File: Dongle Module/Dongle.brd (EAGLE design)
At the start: 100 x 50 mm, 74 parts, among them Q2 2.5A/30V, U1 RFM69HCW, U10 74AHC1G125, U2 HALL-EFFECTSMD, U3 HALL-EFFECTSMD, U4 HALL-EFFECTSMD, U5 HALL-EFFECTSMD, U6 BQ27441-G1, U7 BQ24075, U8 ATSAMD21G-A, U9 3.3V, Y1 32.768kHz

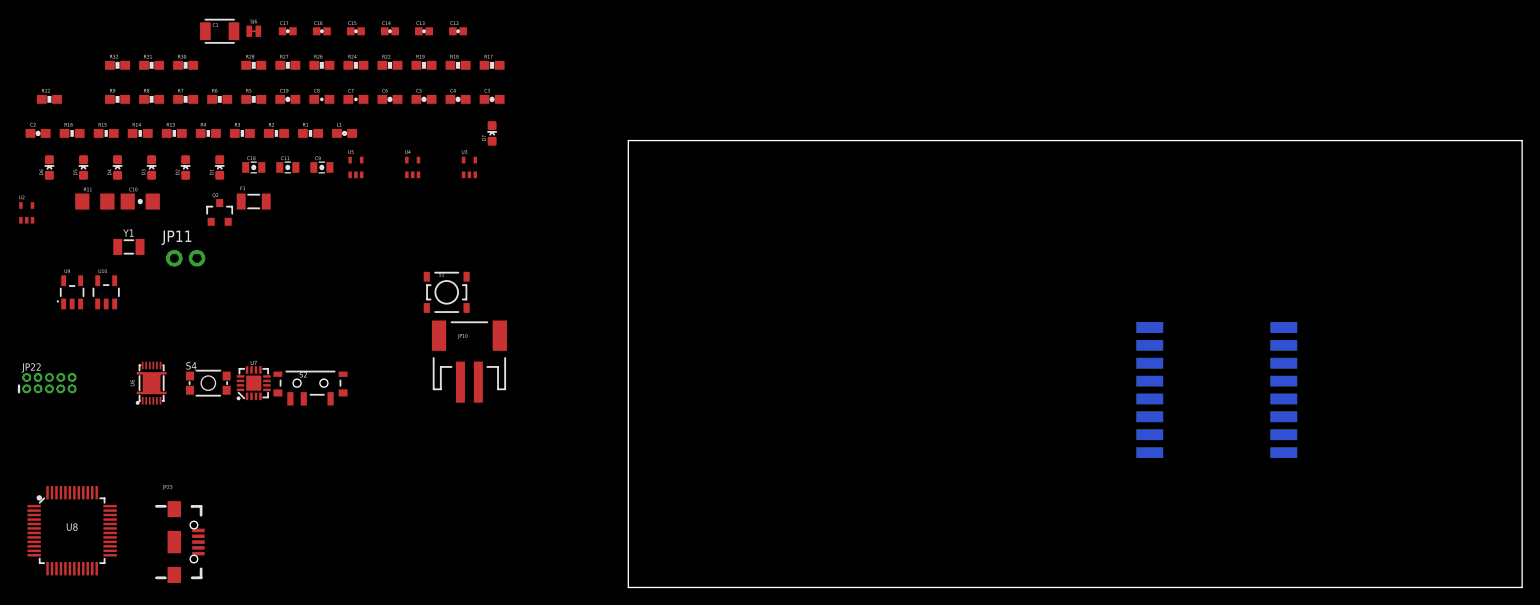
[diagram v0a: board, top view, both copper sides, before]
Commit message: Worked on the laser and dongle schematics Placed the parts on the laser and dongle boards in their rough locations
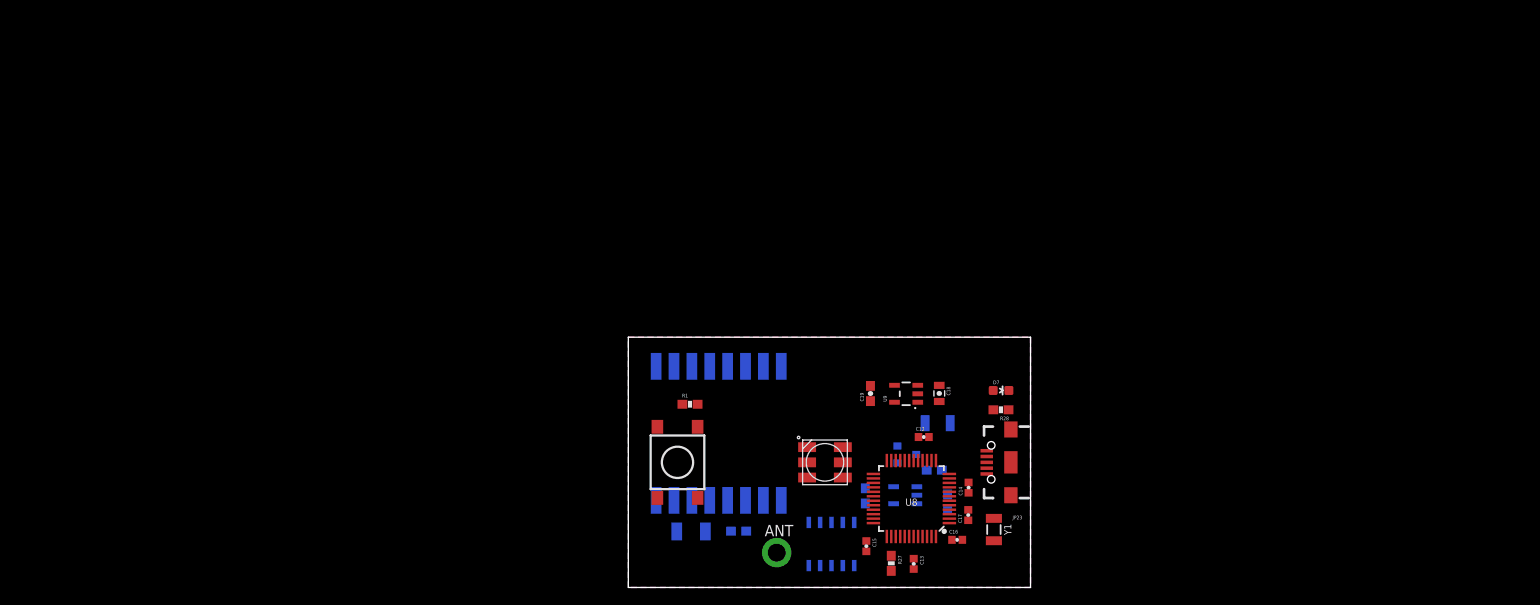
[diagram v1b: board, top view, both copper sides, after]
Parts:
- removed C10: 1.0uF, SparkFun-Capacitors:1206-CAP
- removed C11, C9: 10uF, SparkFun-Capacitors:0805-CAP
- removed C3, C4, C5, C6: 0.1uF, SparkFun-Capacitors:0603-CAP@1
- removed C7: 1.0uF, SparkFun-Capacitors:0603-CAP@2
- removed C8: 0.47uF, SparkFun-Capacitors:0603-CAP@2
- removed D1: BLU, SparkFun-LED:LED-0603
- removed D2, D6: RED, SparkFun-LED:LED-0603
- removed D3: GREEN, SparkFun-LED:LED-0603
- removed D4: WHT, SparkFun-LED:LED-0603
- removed D5: BLUE, SparkFun-LED:LED-0603
- removed JP10: (no value), SparkFun-Connectors:JST-2-SMD
- removed JP11: (no value), mike-temp:1X02_NO_SILK
- removed L1: FB - 30Ohm, SparkFun-Passives:0603
- removed R11: 0.01, SparkFun-Resistors:1206
- removed R12: 1.1k, SparkFun-Passives:0603-RES
- removed R13, R14: 4.7K, SparkFun-Resistors:0603-RES@2
- removed R15, R2, R3, R4: 180, SparkFun-Resistors:0603-RES@2
- removed R16: 1K, SparkFun-Resistors:0603-RES@2
- removed R17, R24: 100k, SparkFun-Resistors:0603-RES
- removed R18, R19, R22, R26: 10K, SparkFun-Resistors:0603-RES
- removed R5, R6, R7, R8, R9: 10K, SparkFun-Resistors:0603-RES@1
- removed S2: (no value), SparkFun-Electromechanical:SWITCH-SPST-SMD-A
- removed S4: RESET, samd21-temp:TACTILE_SWITCH_SMD_4.6X2.8MM
- removed SJ6: PWR-LED, SparkFun-Passives:PAD-JUMPER-2-NC_BY_TRACE_NO_SILK
- removed U2, U3, U4, U5: HALL-EFFECTSMD, SparkFun-Sensors:SC70
- removed U6: BQ27441-G1, battery-management-temp:PDSO-N12
- removed U7: BQ24075, battery-management-temp:PVQFN-N16
- added ANT: (no value), SparkFun-Connectors:1X01_2MM
- added U$1: APA102, SAUVE:APA102
- JP22: value CORTEX_DEBUGPTH -> CORTEX_DEBUGSMD; device samd21-temp:2X5-PTH-1.27MM -> SparkFun-Connectors:SAMTECH_FTSH-105-01
- R1: value 180 -> 330; device SparkFun-Resistors:0603-RES@2 -> SparkFun-Resistors:0603-RES
- S1: value SWITCH-MOMENTARY-2SMD-2 -> SWITCH-MOMENTARY-2SMD-4; device SparkFun-Electromechanical:TACTILE_SWITCH_SMD-2 -> SparkFun-Electromechanical:TACTILE_SWITCH_TALL
- moved Y1 101.8 mm to (40.9, 6.48), turned to 270 degrees
- moved R31 101.6 mm to (35.7, 9.56), flipped to the bottom, turned to 90 degrees
- moved R32 96.5 mm to (26.5, 10.2), flipped to the bottom, turned to 90 degrees
- moved R30 95.2 mm to (34.2, 13.1), flipped to the bottom
- moved JP23 94.0 mm to (42.8, 14.0), turned to 180 degrees
- moved U9 94.0 mm to (31.1, 21.7), turned to 90 degrees
- moved U8 94.0 mm to (31.7, 9.95), turned to 180 degrees
- moved C17 93.4 mm to (38.0, 8.10), turned to 90 degrees
- moved U10 92.2 mm to (31.0, 10.3), flipped to the bottom, turned to 270 degrees
- moved R28 92.1 mm to (41.7, 19.9), turned to 180 degrees
- moved C16 91.0 mm to (36.8, 5.33)
- moved C2 90.1 mm to (12.3, 6.30), flipped to the bottom, turned to 180 degrees
- moved JP22 89.3 mm to (22.7, 4.86), flipped to the bottom
- moved R27 87.5 mm to (29.4, 2.70), turned to 270 degrees
- moved C14 82.5 mm to (38.1, 11.2), turned to 90 degrees
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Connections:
- removed net !CE!: R17.1, U7.4
- removed net !CHG!: R15.2, U7.9
- removed net !PGOOD!: R16.2, U7.7
- removed net 1.8V: C8.1, U6.5
- removed net A0: U8.3
- removed net A1: U8.7
- removed net A2: U8.8
- removed net A3: U8.9
- removed net AREF: U8.4
- removed net BATTERY_IN: C7.1, JP10.2, R11.2, U6.6, U6.8
- removed net BLU_PWM: R4.1
- removed net BMS_SCL: R14.1, U6.2
- removed net BMS_SDA: R13.1, U6.1
- removed net D0/RXI: U8.16
- removed net D1/TXO: U8.15
- removed net D10/SS: U8.27
- removed net D11/MOSI: U8.25
- removed net D12/MISO: U8.28
- removed net D13/SCK: U8.26
- removed net D2: U8.23
- removed net D3: U8.14
- removed net D4: U8.13
- removed net D5: U8.24
- removed net D6: U8.29
- removed net D7: U8.30
- removed net D8: U8.11
- removed net D9: U8.12
- removed net EN1: R18.2, U7.6
- removed net EN2: U7.5
- removed net GPOUT: R26.1, U6.12
- removed net GRN_PWM: R2.1
- removed net HALL_DWN: R7.2, U3.5
- removed net HALL_LFT: R8.2, U4.5
- removed net HALL_RHT: R9.2, U5.5
- removed net HALL_UP: R6.2, U2.5
- removed net ILIM: R12.1, U7.12
- removed net N$1: D3.A, R2.2
- removed net N$11: D5.C, R15.1
- removed net N$12: D6.C, R16.1
- removed net N$2: D2.A, R3.2
- removed net N$23: D7.C, SJ6.2
- removed net N$3: D1.A, R4.2
- removed net N$4: D4.A, R1.2
- removed net N$5: R24.2, S2.1
- removed net OUT: C9.1, D5.A, D6.A, R13.2, R14.2, R18.1, R19.1, R26.2, U7.10, U7.11
- removed net RED_PWM: R3.1
- removed net RF_NSS: U1.5
- removed net RX_LED: U8.48
- removed net SCL: U8.32
- removed net SDA: U8.31
- removed net SYSOFF: S2.2, U7.15
- removed net TRK_BTN: R5.2, S1.1
- removed net TS: R22.2, U6.10, U7.1
- removed net TX_LED: U8.39
- removed net VCC: C3.1, C4.1, C5.1, C6.1, R5.1, R6.1, R7.1, R8.1, R9.1, U2.4, U3.4, U4.4, U5.4
- removed net V_BATT: C11.1, R11.1, R24.1, U6.7, U7.2, U7.3
- removed net WHT_PWM: R1.1
- new net APA_CLK: U$1.CKI, U8.14
- new net APA_MOSI: U$1.SDI, U8.13
- new net RF_SS: U1.5, U8.27
- new net SEL_BTN: R1.2, S1.A2, U8.24
- net !RESET: no longer S4.3, S4.4
- net 3.3V: now also S1.B2, U$1.VCC; no longer L1.1
- net ANT: now also ANT.1
- net GND: now also D7.C, R1.1, U$1.GND; no longer C10.2, C11.2, C3.2, C4.2, C5.2, C6.2, C7.2, C8.2, C9.2, D1.C, D2.C, D3.C, D4.C, JP10.1, JP11.2, R12.2, R17.2, R19.2, R22.1, S1.2, S2.3, S4.1, S4.2, SJ6.1, U2.2, U3.2, U4.2, U5.2, U6.3, U6.EP, U6.EP1, U6.EP2, U6.EP3, U6.EP4, U7.14, U7.8, U7.EP
- net RF_MISO: now also U8.28
- net RF_MOSI: now also U8.25
- net RF_SCK: now also U8.26
- net VDDANA: no longer L1.2
- net V_USB: no longer C10.1, JP11.1, U7.13
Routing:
- added copper zone on layer 1, net GND
- added copper zone on layer 16, net GND
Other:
- board size 100 x 50 mm -> 45 x 28 mm

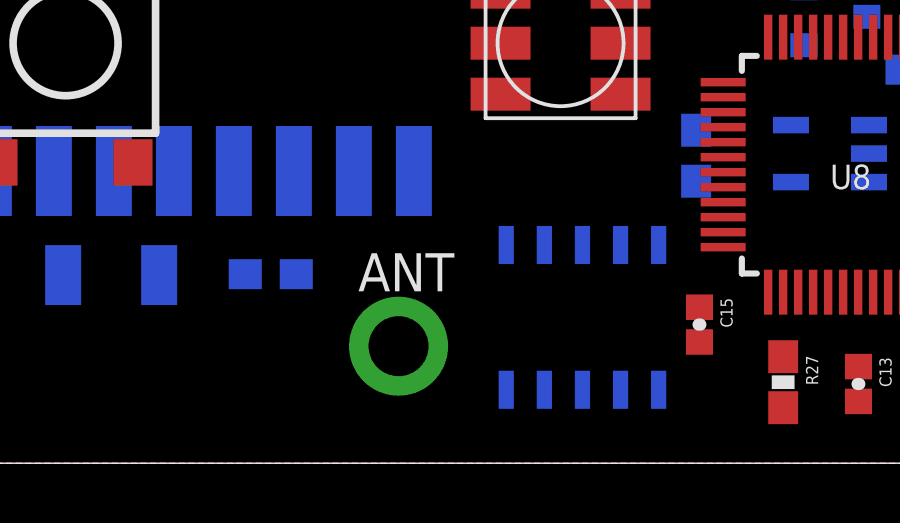
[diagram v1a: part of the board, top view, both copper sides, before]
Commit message: Created, placed, and routed a starter board for the Camera Module
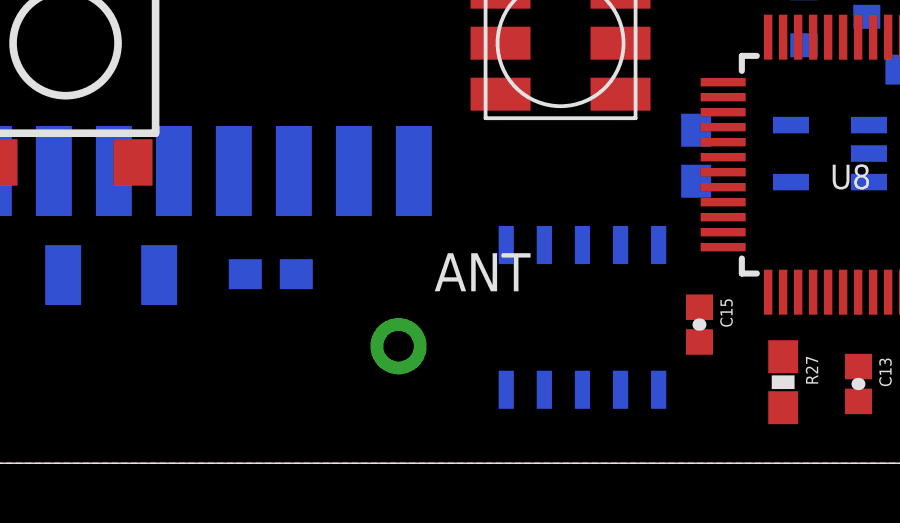
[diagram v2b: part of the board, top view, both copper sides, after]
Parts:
- ANT: device SparkFun-Connectors:1X01_2MM -> SparkFun-Connectors:1X01_NO_SILK
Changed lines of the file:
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@@
 <attribute name="VALUE" x="18.7" y="9.9" size="1.27" layer="27" font="vector"/>
 </element>
-<element name="ANT" library="SparkFun-Connectors" package="1X01_2MM" value="" x="16.6" y="3.9"/>
+<element name="ANT" library="SparkFun-Connectors" package="1X01_NO_SILK" value="" x="16.6" y="3.9"/>
 </elements>
 <signals>

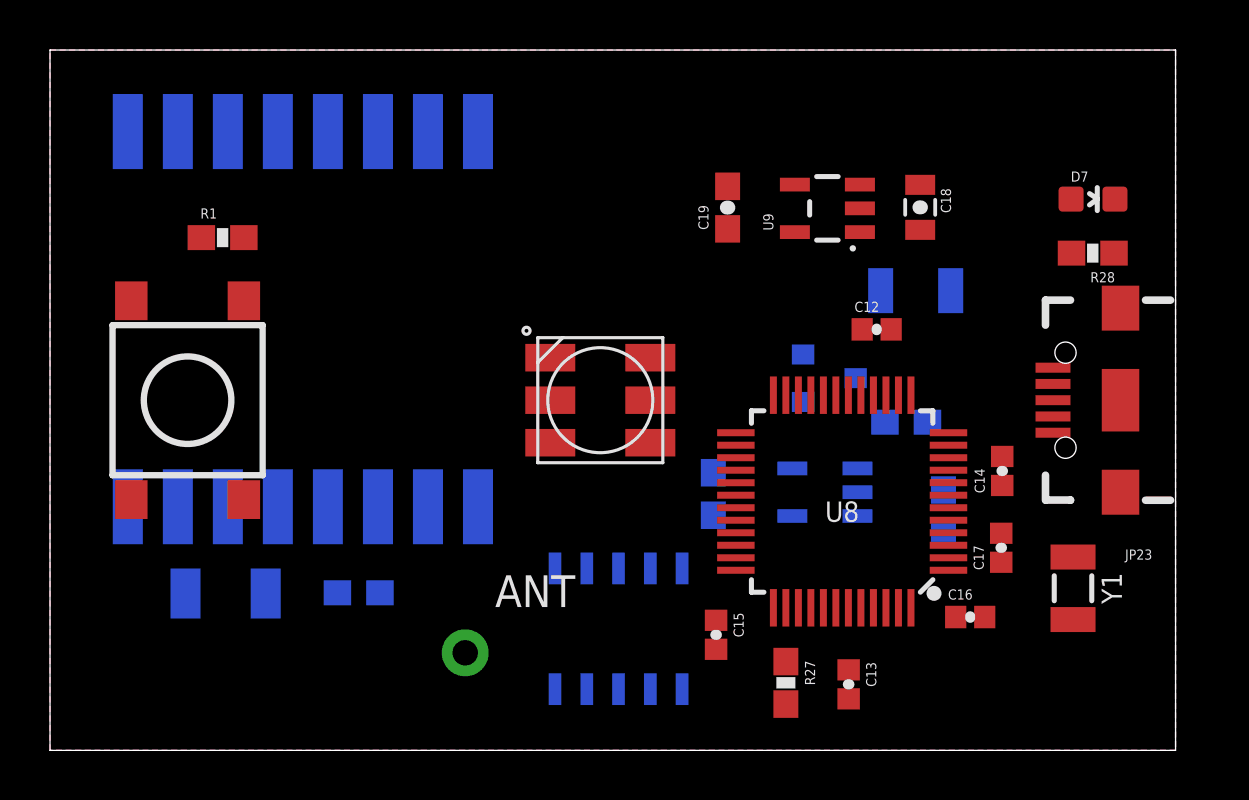
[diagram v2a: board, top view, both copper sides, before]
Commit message: Routed the dongle and camera modules
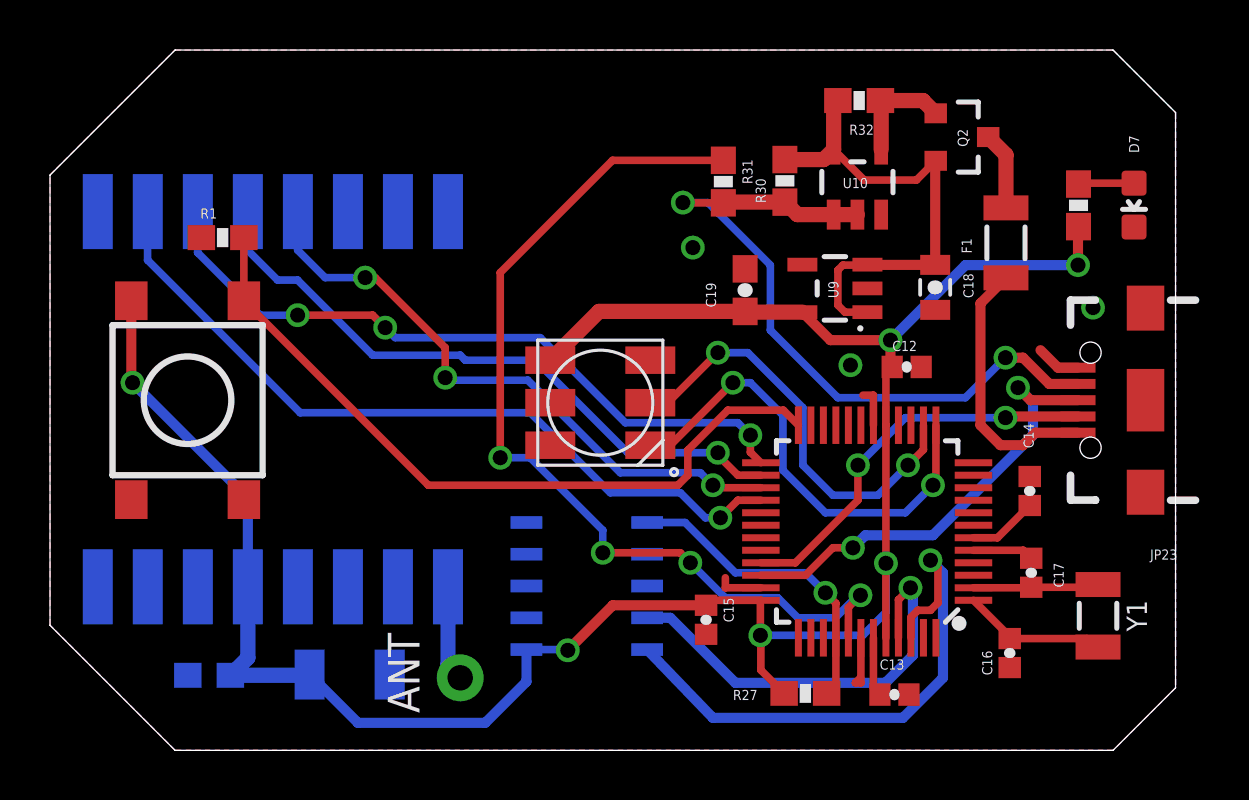
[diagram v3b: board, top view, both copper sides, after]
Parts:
- moved R32 16.8 mm to (32.4, 26.0), flipped to the top, turned to 180 degrees
- moved R31 15.8 mm to (26.9, 22.7), flipped to the top, turned to 270 degrees
- moved U10 12.5 mm to (32.3, 22.7), flipped to the top, turned to 0 degrees
- moved Q2 11.0 mm to (36.4, 24.5), flipped to the top, turned to 270 degrees
- moved R30 10.8 mm to (29.4, 22.8), flipped to the top, turned to 90 degrees
- moved C2 6.83 mm to (6.36, 3.00), turned to 0 degrees
- moved C1 5.92 mm to (12.0, 3.03), turned to 180 degrees
- moved F1 4.08 mm to (38.2, 20.3), flipped to the top, turned to 90 degrees
- moved U1 3.42 mm to (8.91, 14.0)
- moved C19 3.37 mm to (27.8, 18.4)
- moved C18 3.26 mm to (35.4, 18.5)
- moved U9 3.21 mm to (31.4, 18.5)
- moved C16 2.14 mm to (38.4, 3.89), turned to 90 degrees
- moved JP22 2.13 mm to (21.5, 6.57), turned to 90 degrees
- moved R28 1.99 mm to (41.1, 21.8), turned to 270 degrees
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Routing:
- net 3.3V: track 0.00 -> 90.9 mm, vias 0 -> 6
- net USB_HOST_EN: track 0.00 -> 38.0 mm, vias 0 -> 4
- net RF_MISO: track 0.00 -> 31.0 mm, vias 0 -> 1
- net SEL_BTN: track 0.00 -> 29.8 mm
- net N$19: track 0.00 -> 28.9 mm, vias 0 -> 2
- net RF_MOSI: track 0.00 -> 28.0 mm, vias 0 -> 3
- net RF_SCK: track 0.00 -> 25.9 mm, vias 0 -> 1
- net RF_SS: track 0.00 -> 24.7 mm, vias 0 -> 3
- net SWDIO: track 0.00 -> 22.5 mm, vias 0 -> 1
- net VIN: track 0.00 -> 19.9 mm
- net APA_MOSI: track 0.00 -> 18.7 mm, vias 0 -> 2
- net USB_D+: track 0.00 -> 18.0 mm, vias 0 -> 2
- net APA_CLK: track 0.00 -> 17.2 mm, vias 0 -> 2
- net SWCLK: track 0.00 -> 17.1 mm, vias 0 -> 1
- net USB_D-: track 0.00 -> 15.9 mm, vias 0 -> 2
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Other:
- outline, holes or cut-outs redrawn
